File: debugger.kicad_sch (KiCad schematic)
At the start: 0 parts

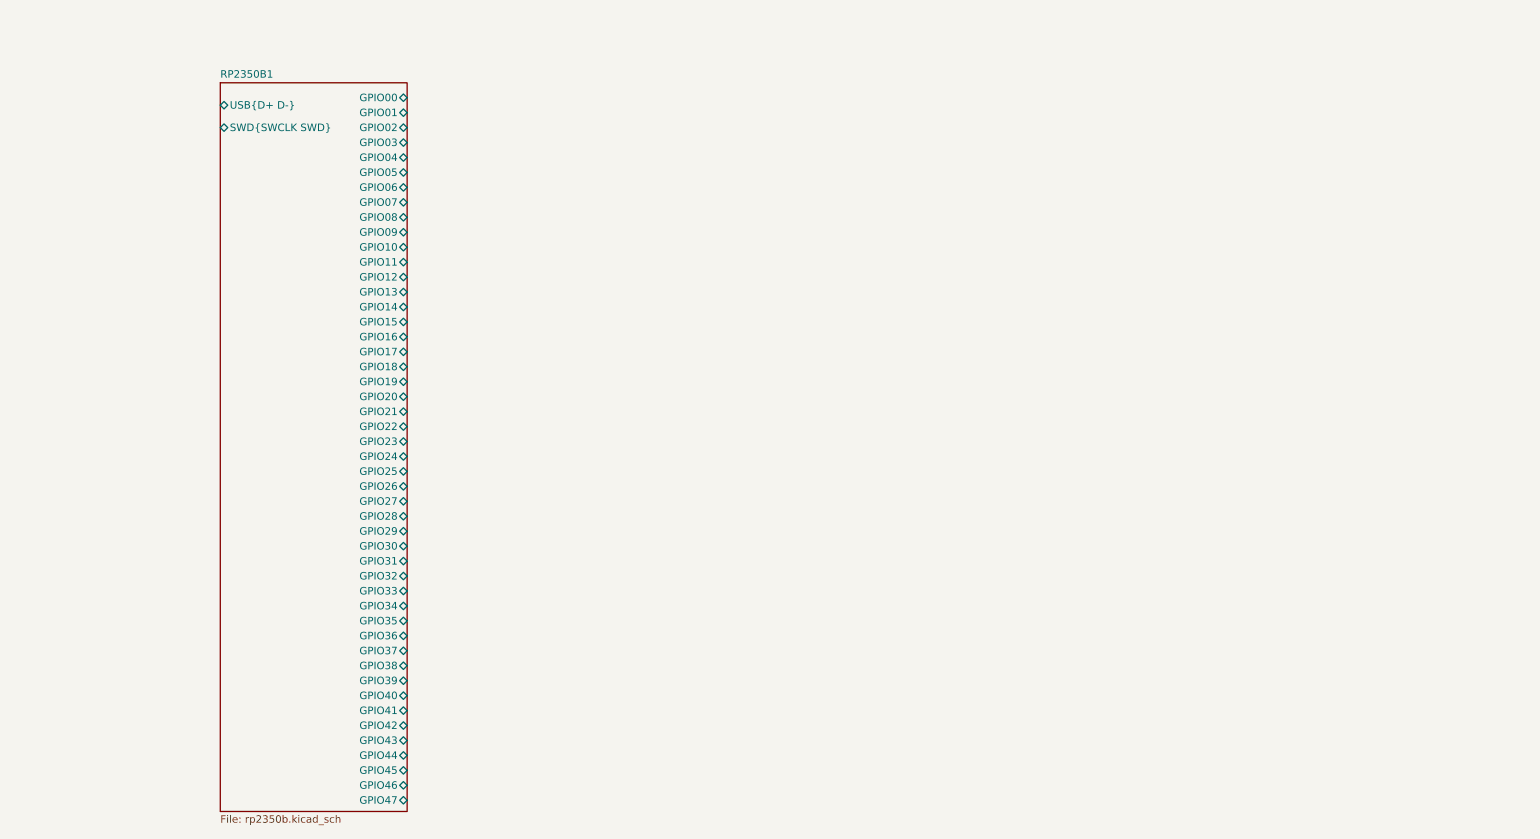
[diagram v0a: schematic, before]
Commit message: Do pin assignment for tester
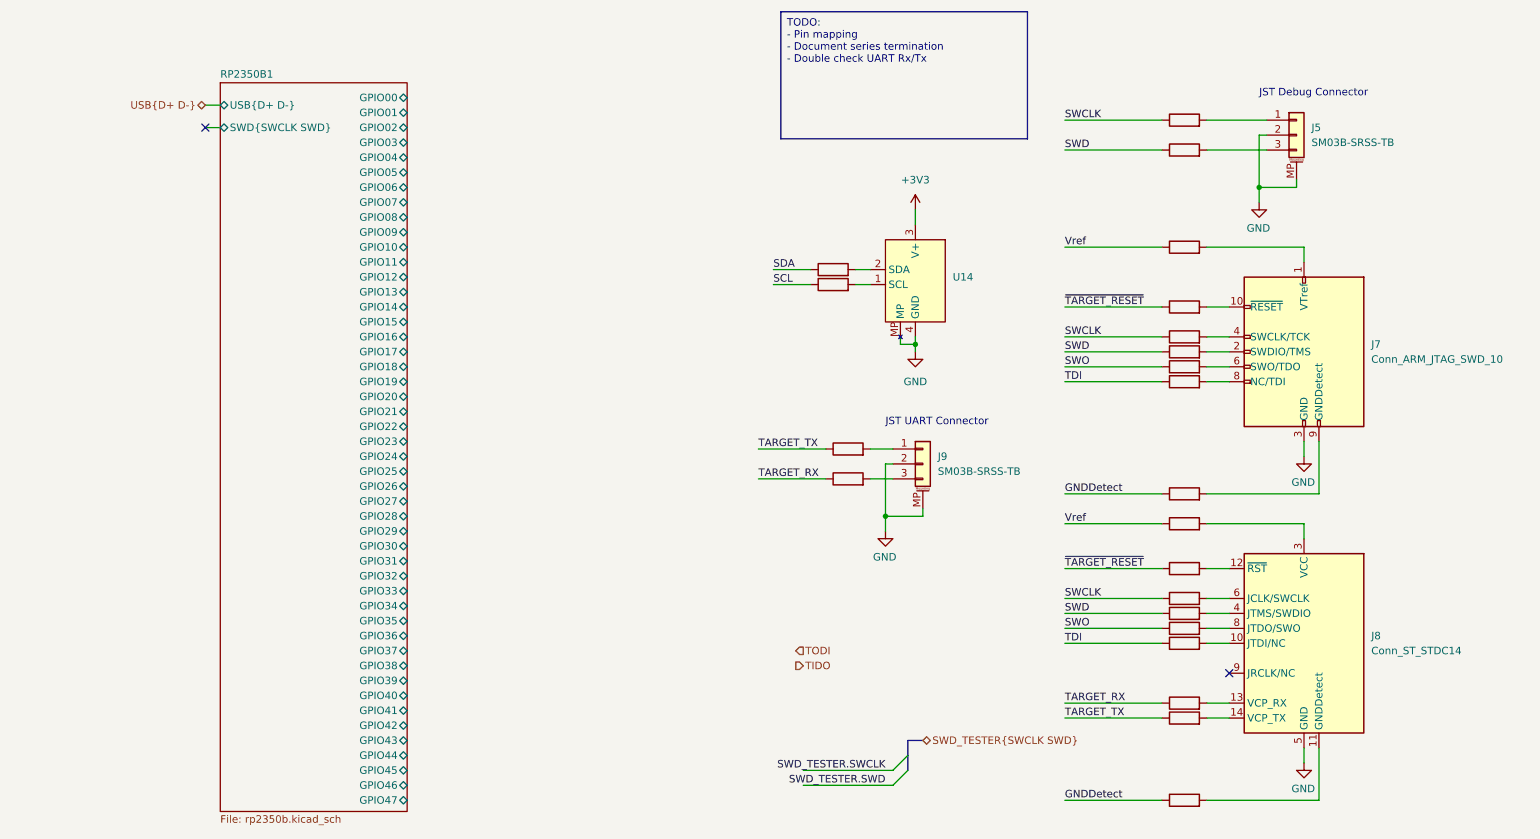
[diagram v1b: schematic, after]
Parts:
- added J5, J9: SM03B-SRSS-TB, Connector_JST:JST_SH_SM03B-SRSS-TB_1x03-1MP_P1.00mm_Horizontal, symbol Connector_Generic_MountingPin:Conn_01x03_MountingPin
- added J7: Conn_ARM_JTAG_SWD_10, Connector_PinHeader_1.27mm:PinHeader_2x05_P1.27mm_Vertical_SMD, symbol Connector:Conn_ARM_JTAG_SWD_10
- added J8: Conn_ST_STDC14, Connector_PinHeader_1.27mm:PinHeader_2x07_P1.27mm_Vertical_SMD, symbol Connector:Conn_ST_STDC14
- added R69, R70, R71, R72, R73, R74, R75, R76, R77, R78, R79, R80, R81, R82, R83, R84, R85, R86, R87, R88, R89, R90: 100R, Resistor_SMD:R_0402_1005Metric_Pad0.72x0.64mm_HandSolder, symbol Device:R
- added U14: ~, Connector_JST:JST_SH_SM04B-SRSS-TB_1x04-1MP_P1.00mm_Horizontal, symbol Project_Specific:StemmaQtTarget
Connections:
- new net: J5.1 (Pin_1), R85.2
- new net: J8.11 (GNDDetect), R84.2
- new net: J8.12 (~{RST}), R76.2
- new net: J8.6 (JCLK/SWCLK), R77.2
- new net: J8.8 (JTDO/SWO), R79.2
- new net: J7.8 (NC/TDI), R74.2
- new net: J7.6 (SWO/TDO), R73.2
- new net: J8.10 (JTDI/NC), R80.2
- new net: J8.13 (VCP_RX), R82.2
- new net: J8.14 (VCP_TX), R83.2
- new net: J8.3 (VCC), R75.2
- new net: J8.4 (JTMS/SWDIO), R78.2
- new net: J7.1 (VTref), R69.2
- new net: J7.10 (~{RESET}), R70.2
- new net: J7.2 (SWDIO/TMS), R72.2
- new net: J7.4 (SWCLK/TCK), R71.2
- new net: J7.9 (GNDDetect), R81.2
- new net: R90.2, U14.1 (SCL)
- new net: R89.2, U14.2 (SDA)
- new net: J5.3 (Pin_3), R86.2
- new net: J9.1 (Pin_1), R87.2
- new net: J9.3 (Pin_3), R88.2
- new net +3V3: U14.3 (V+)
- new net GND: J5.2 (Pin_2), J5.MP (MountPin), J7.3 (GND), J7.5 (GND), J8.5 (GND), J8.7 (GND), J9.2 (Pin_2), J9.MP (MountPin), U14.4 (GND), U14.MP
- new net GNDDetect: R81.1, R84.1
- new net SCL: R90.1
- new net SDA: R89.1
- new net SWCLK: R71.1, R77.1, R85.1
- new net SWD: R72.1, R78.1, R86.1
- new net SWO: R73.1, R79.1
- new net TARGET_RX: R82.1, R88.1
- new net TARGET_TX: R83.1, R87.1
- new net TDI: R74.1, R80.1
- new net Vref: R69.1, R75.1
- new net ~{TARGET_RESET}: R70.1, R76.1
- no-connect marks 0 -> 2
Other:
- note added: "JST Debug Connector"
- note added: "JST UART Connector"

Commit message: Start Layout
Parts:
- added D7: LED, LED_SMD:LED_0805_2012Metric, symbol Device:LED
- added R97: 470R, Resistor_SMD:R_0402_1005Metric_Pad0.72x0.64mm_HandSolder, symbol Device:R
- J8, R75, R76, R77, R78, R79, R80, R82, R83, R84: now not fitted
- U14: symbol Project_Specific:StemmaQtTarget -> Project_Specific:StemmaQtController
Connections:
- net GND: now also R97.1
- net RP2350B1/GPIO25: now also D7.2 (A)
- new net: D7.1 (K), R97.2
- no-connect marks 2 -> 34
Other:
- note added: "100R"
- note added: "Note: Pin Mapping based on the board_pico_config.h for the pico probe"

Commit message: Layout Tester and USB Hub
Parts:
- removed J8: Conn_ST_STDC14, Connector_PinHeader_1.27mm:PinHeader_2x07_P1.27mm_Vertical_SMD, symbol Connector:Conn_ST_STDC14
- removed R75, R76, R77, R78, R79, R80, R82, R83, R84: 100R, Resistor_SMD:R_0402_1005Metric_Pad0.72x0.64mm_HandSolder, symbol Device:R
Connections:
- no-connect marks 34 -> 33

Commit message: WIP
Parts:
- J5, J9: value SM03B-SRSS-TB -> BM03B-SRSS-TB; footprint Connector_JST:JST_SH_SM03B-SRSS-TB_1x03-1MP_P1.00mm_Horizontal -> Connector_JST:JST_SH_BM03B-SRSS-TB_1x03-1MP_P1.00mm_Vertical; LCSC (none) -> C160389
- J7: LCSC (none) -> C42372555
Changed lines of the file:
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@@
+			)
+		)
+		(property "LCSC" "C42372555"
+			(at 245.11 81.28 0)
+			(effects
+				(font
+					(size 1.27 1.27)
+				)
+				(hide yes)
 			)
 		)
@@
 			)
 		)
-		(property "Value" "SM03B-SRSS-TB"
+		(property "Value" "BM03B-SRSS-TB"
 			(at 246.38 45.72 0)
 			(effects
@@
 			)
 		)
-		(property "Footprint" "Connector_JST:JST_SH_SM03B-SRSS-TB_1x03-1MP_P1.00mm_Horizontal"
+		(property "Footprint" "Connector_JST:JST_SH_BM03B-SRSS-TB_1x03-1MP_P1.00mm_Vertical"
 			(at 243.84 44.45 0)
 			(effects
@@
 		)
 		(property "Description" ""
+			(at 243.84 44.45 0)
+			(effects
+				(font
+					(size 1.27 1.27)
+				)
+				(hide yes)
+			)
+		)
+		(property "LCSC" "C160389"
 			(at 243.84 44.45 0)
 			(effects
@@
 			)
 		)
-		(property "Value" "SM03B-SRSS-TB"
+		(property "Value" "BM03B-SRSS-TB"
 			(at 182.88 101.6 0)
 			(effects
@@
 			)
 		)
-		(property "Footprint" "Connector_JST:JST_SH_SM03B-SRSS-TB_1x03-1MP_P1.00mm_Horizontal"
+		(property "Footprint" "Connector_JST:JST_SH_BM03B-SRSS-TB_1x03-1MP_P1.00mm_Vertical"
 			(at 180.34 100.33 0)
 			(effects
@@
 			(at 180.34 100.33 0)
 			(effects
+				(font
+					(size 1.27 1.27)
+				)
+				(hide yes)
+			)
+		)
+		(property "LCSC" "C160389"
+			(at 180.34 100.33 0)
+			(effects

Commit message: JLC rotations
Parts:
- J5, J9: FT Rotation Offset (none) -> 180
- J7: FT Rotation Offset (none) -> -90
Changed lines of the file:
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@@
+			)
+		)
+		(property "FT Rotation Offset" ""
+			(at 224.79 41.91 90)
+			(effects
+				(font
+					(size 1.27 1.27)
+				)
+				(hide yes)
 			)
 		)
@@
 			)
 		)
+		(property "FT Rotation Offset" ""
+			(at 224.79 86.36 90)
+			(effects
+				(font
+					(size 1.27 1.27)
+				)
+				(hide yes)
+			)
+		)
 		(pin "1"
 		)
@@
 			)
 		)
+		(property "FT Rotation Offset" ""
+			(at 224.79 83.82 90)
+			(effects
+				(font
+					(size 1.27 1.27)
+				)
+				(hide yes)
+			)
+		)
 		(pin "1"
 		)
@@
 			)
 		)
+		(property "FT Rotation Offset" ""
+			(at 118.11 111.76 0)
+			(effects
+				(font
+					(size 1.27 1.27)
+				)
+				(hide yes)
+			)
+		)
 		(pin "1"
 		)
@@
 			)
 		)
+		(property "FT Rotation Offset" "-90"
+			(at 245.11 81.28 0)
+			(effects
+				(font
+					(size 1.27 1.27)
+				)
+				(hide yes)
+			)
+		)
 		(pin "7"
 		)
@@
 			)
 		)
+		(property "FT Rotation Offset" ""
+			(at 179.07 68.58 0)
+			(effects
+				(font
+					(size 1.27 1.27)
+				)
+				(hide yes)
+			)
+		)
 		(pin "1"
 		)
@@
 			)
 		)
+		(property "FT Rotation Offset" ""
+			(at 224.79 78.74 90)
+			(effects
+				(font
+					(size 1.27 1.27)
+				)
+				(hide yes)
+			)
+		)
 		(pin "1"
 		)
@@
 			)
 		)
+		(property "FT Rotation Offset" ""
+			(at 224.79 63.5 90)
+			(effects
+				(font
+					(size 1.27 1.27)
+				)
+				(hide yes)
+			)
+		)
 		(pin "1"
 		)
@@
 			)
 		)
+		(property "FT Rotation Offset" "180"
+			(at 243.84 44.45 0)
+			(effects
+				(font
+					(size 1.27 1.27)
+				)
+				(hide yes)
+			)
+		)
 		(pin "1"
 		)
@@
 			)
 		)
+		(property "FT Rotation Offset" ""
+			(at 118.11 121.92 90)
+			(effects
+				(font
+					(size 1.27 1.27)
+				)
+				(hide yes)
+			)
+		)
 		(pin "1"
 		)
@@
 			)
 		)
+		(property "FT Rotation Offset" ""
+			(at 224.79 105.41 90)
+			(effects
+				(font
+					(size 1.27 1.27)
+				)
+				(hide yes)
+			)
+		)
 		(pin "1"
 		)
@@
 			)
 		)
+		(property "FT Rotation Offset" ""
+			(at 224.79 73.66 90)
+			(effects
+				(font
+					(size 1.27 1.27)
+				)
+				(hide yes)
+			)
+		)
 		(pin "1"
 		)
@@
 			)
 		)
+		(property "FT Rotation Offset" ""
+			(at 165.1 69.85 90)
+			(effects
+				(font
+					(size 1.27 1.27)
+				)
+				(hide yes)
+			)
+		)
 		(pin "1"
 		)
@@
 			)
 		)
+		(property "FT Rotation Offset" ""
+			(at 224.79 46.99 90)
+			(effects
+				(font
+					(size 1.27 1.27)
+				)
+				(hide yes)
+			)
+		)
 		(pin "1"
 		)
@@
 			)
 		)
+		(property "FT Rotation Offset" ""
+			(at 167.64 97.79 90)
+			(effects
+				(font
+					(size 1.27 1.27)
+				)
+				(hide yes)
+			)
+		)
 		(pin "1"
 		)
@@
 			)
 		)
+		(property "FT Rotation Offset" "180"
+			(at 180.34 100.33 0)
+			(effects
+				(font
+					(size 1.27 1.27)
+				)
+				(hide yes)
+			)
+		)
 		(pin "1"
 		)
@@
 			)
 		)
+		(property "FT Rotation Offset" ""
+			(at 165.1 67.31 90)
+			(effects
+				(font
+					(size 1.27 1.27)
+				)
+				(hide yes)
+			)
+		)
 		(pin "1"
 		)
@@
 			)
 		)
+		(property "FT Rotation Offset" ""
+			(at 224.79 81.28 90)
+			(effects
+				(font
+					(size 1.27 1.27)
+				)
+				(hide yes)
+			)
+		)
 		(pin "1"
 		)
@@
 			(at 167.64 102.87 90)
 			(effects
+				(font
+					(size 1.27 1.27)
+				)
+				(hide yes)
+			)
+		)
+		(property "FT Rotation Offset" ""
+			(at 167.64 102.87 90)
+			(effects

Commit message: Fix JTAG IDC
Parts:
- J7: footprint Connector_PinHeader_1.27mm:PinHeader_2x05_P1.27mm_Vertical_SMD -> ProjectSpecific:PinHeader_2x05_P1.27mm_Vertical_SMD_IDC
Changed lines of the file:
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@@
 			)
 		)
-		(property "Footprint" "Connector_PinHeader_1.27mm:PinHeader_2x05_P1.27mm_Vertical_SMD"
+		(property "Footprint" "ProjectSpecific:PinHeader_2x05_P1.27mm_Vertical_SMD_IDC"
 			(at 245.11 81.28 0)
 			(effects

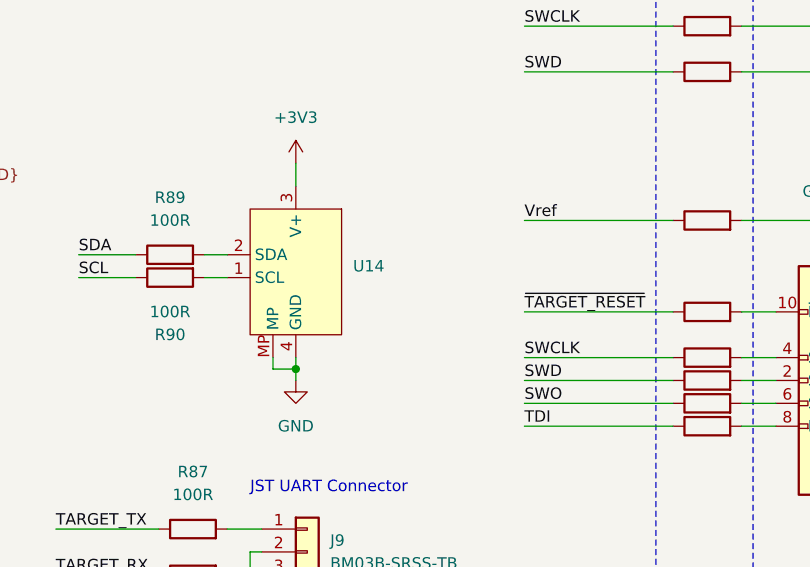
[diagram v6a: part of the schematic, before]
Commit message: Address board review comments
- Add pull-ups for both I2C busses (4K7)
- Set eFuse limit to 600mA (400mA before)
- Label StemmaQt as such in schematics
- Fix typo in USB Port value
- Fix USB Mux to be disabled by default (pull-down to pull-up)
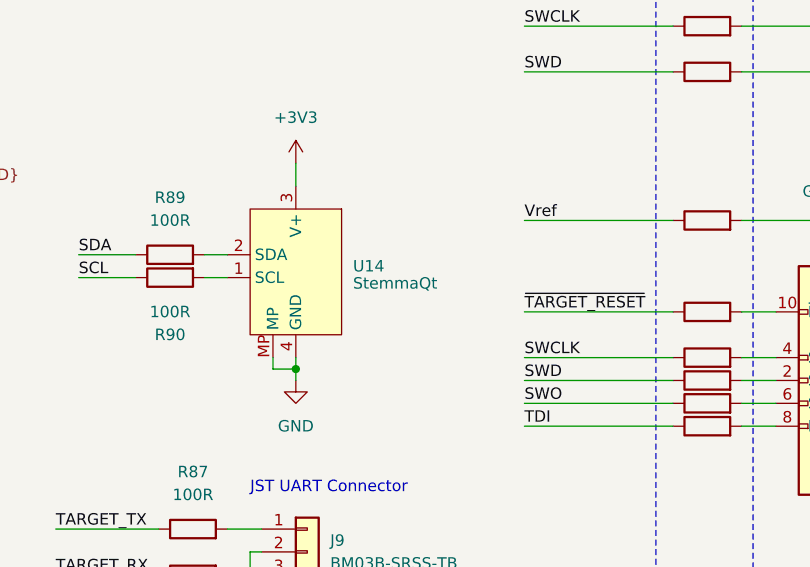
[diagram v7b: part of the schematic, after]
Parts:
- U14: value ~ -> StemmaQt
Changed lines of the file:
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@@
 			)
 		)
-		(property "Value" "~"
+		(property "Value" "StemmaQt"
 			(at 185.42 70.485 0)
 			(effects
